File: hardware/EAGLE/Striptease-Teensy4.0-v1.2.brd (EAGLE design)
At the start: 48.3 x 114.3 mm, 18 parts, among them IC1 74245N

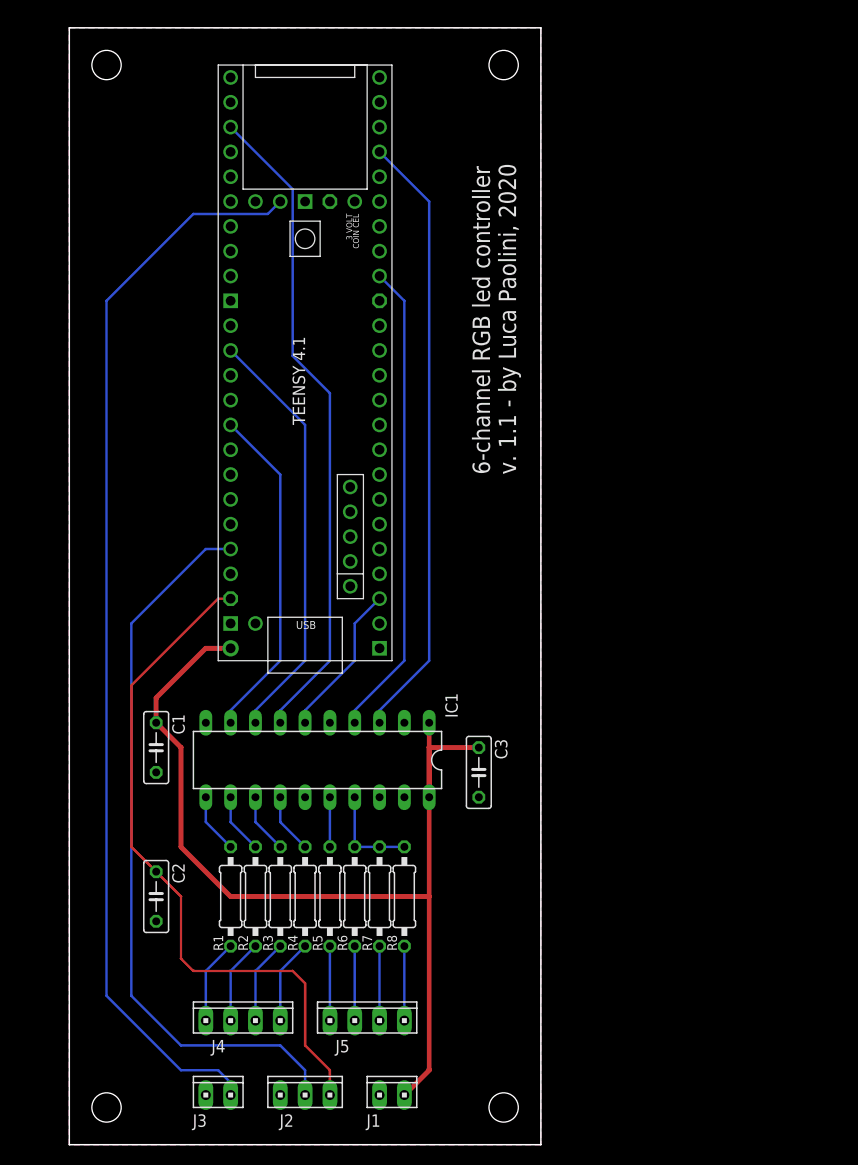
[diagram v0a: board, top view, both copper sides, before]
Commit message: Change connector names in EAGLE boards.
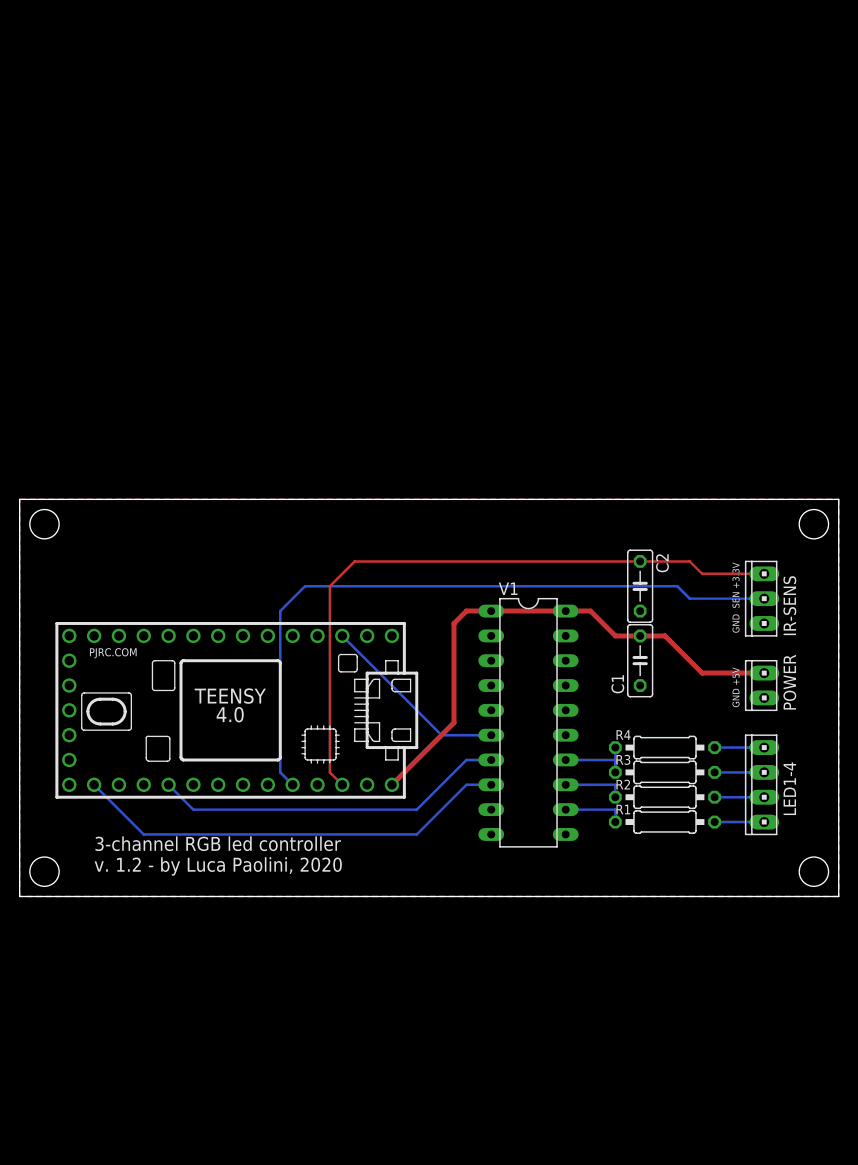
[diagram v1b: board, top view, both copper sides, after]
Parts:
- removed C3: 100n, rcl:C050-025X075
- removed IC1: 74245N, 74ttl-din:DIL20
- removed J1, J3: (no value), con-amp:10X02MTA
- removed J2: (no value), con-amp:10X03MTA
- removed J4, J5: (no value), con-amp:10X04MTA
- removed R5, R6, R7, R8: 100, rcl:0207/10
- removed U$3: TEENSY41-E, teensy:TENNSY41-E
- added IR-SENS: (no value), con-amp:10X03MTA
- added LED1-4: (no value), con-amp:10X04MTA
- added POWER: (no value), con-amp:10X02MTA
- added U$1: TEENSY_4.0-BASIC, Teensy-4.0:TEENSY_4.0-BASIC
- added V1: 74245N, 74ttl-din:DIL20
- moved C2 58.8 mm to (62.2, 53.3)
- moved C1 50.3 mm to (62.2, 45.7), turned to 90 degrees
- moved R1 45.1 mm to (64.8, 29.2), turned to 0 degrees
- moved R2 43.1 mm to (64.8, 31.8), turned to 0 degrees
- moved R3 41.4 mm to (64.8, 34.3), turned to 0 degrees
- moved R4 39.9 mm to (64.8, 36.8), turned to 0 degrees
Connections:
- removed net N$16: IC1.14, R4.1
- removed net N$19: J4.1, R4.2
- removed net N$20: J5.4, R5.2
- removed net N$22: J5.3, R6.2
- removed net N$23: IC1.9, U$3.17-A3/TX4/SDA1
- removed net N$24: IC1.8, U$3.14-A0/TX3/SPDIF_OUT
- removed net N$25: IC1.7, U$3.35-TX8
- removed net N$26: IC1.6, U$3.1-TX1/MISO1/CTX2
- removed net N$27: IC1.4, U$3.24-A10/TX6/SCL2
- removed net N$28: IC1.3, U$3.29-TX7
- removed net N$3: IC1.16, R5.1
- removed net N$31: J2.2, U$3.22-A8/CTX1
- removed net N$6: J5.2, R7.2
- new net N$21: U$1.1/TX, V1.6
- new net N$5: LED1-4.1, R4.2
- net +5V: now also C1.2, POWER.1, U$1.VIN, V1.1, V1.20; no longer C1.1, C3.1, IC1.1, IC1.20, J1.1, U$3.VIN
- net GND: now also C1.1, IR-SENS.3, POWER.2, U$1.GND, U$1.GND2, V1.10, V1.19, V1.2, V1.3, V1.4, V1.5, V1.9; no longer C1.2, C3.2, IC1.10, IC1.19, IC1.2, IC1.5, J1.2, J2.3, J3.2, U$3.GND1, U$3.GND2, U$3.GND3, U$3.GND6
- net N$1: now also IR-SENS.2, U$1.22/A8; no longer C2.1, J2.1, U$3.3V3-3
- net N$10: now also U$1.14/A0, V1.8; no longer J5.1, R8.2
- net N$11: now also V1.12; no longer IC1.11
- net N$12: now also V1.13; no longer IC1.12
- net N$13: now also R4.1, V1.14; no longer IC1.13
- net N$14: now also U$1.17/A3, V1.7; no longer IC1.17, R6.1, R7.1, R8.1
- net N$2: now also C2.1, IR-SENS.1, U$1.3V3_LO; no longer J3.1, U$3.PROGRAM
- net N$7: now also LED1-4.2; no longer J4.2
- net N$8: now also LED1-4.3; no longer J4.3
- net N$9: now also LED1-4.4; no longer J4.4
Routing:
- net N$31: track 74.9 -> 0.00 mm
- net N$25: track 67.3 -> 0.00 mm
- net N$28: track 62.6 -> 0.00 mm
- net N$27: track 48.9 -> 0.00 mm
- net +5V: track 102.8 -> 55.3 mm
- net N$2: track 110.8 -> 66.9 mm
- net N$24: track 43.4 -> 0.00 mm
- net N$10: track 7.62 -> 44.8 mm
- net N$23: track 34.7 -> 0.00 mm
- net N$14: track 10.2 -> 36.2 mm
- net N$21: track 0.00 -> 20.7 mm
- net N$26: track 15.9 -> 0.00 mm
- net N$19: track 8.67 -> 0.00 mm
- net N$6: track 7.62 -> 0.00 mm
- net N$22: track 7.62 -> 0.00 mm
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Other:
- board size 48.3 x 114.3 mm -> 83.8 x 40.6 mm
- board text added: "3-channel RGB led controller v. 1.2 - by Luca Paolini, 2020"
- board text added: "GND +5V"
- board text added: "GND SEN +3.3V"
- board text removed: "6-channel RGB led controller v. 1.1 - by Luca Paolini, 2020"

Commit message: Add connector pinout for LEDs in EAGLE boards.
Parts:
- renumbered IR-SENS to IR-RECV
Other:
- board text added: "1 2 3 3"
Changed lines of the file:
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@@
 <text x="72.39" y="48.26" size="0.7" layer="25" font="vector" rot="R90"> GND  SEN +3.3V</text>
 <text x="72.39" y="40.64" size="0.7" layer="25" font="vector" rot="R90"> GND +5V</text>
+<text x="72.39" y="27.94" size="0.9" layer="25" font="vector" rot="R90">  1    2    3    3</text>
 </plain>
 <attributes>
@@
 <attribute name="VALUE" x="72.7791" y="28.0439" size="1.27" layer="27" rot="R90"/>
 </element>
-<element name="IR-SENS" library="con-amp" library_urn="urn:adsk.eagle:library:127" package="10X03MTA" package3d_urn="urn:adsk.eagle:package:8081621/1" value="" x="74.93" y="52.07" smashed="yes" rot="R90">
+<element name="IR-RECV" library="con-amp" library_urn="urn:adsk.eagle:library:127" package="10X03MTA" package3d_urn="urn:adsk.eagle:package:8081621/1" value="" x="74.93" y="52.07" smashed="yes" rot="R90">
 <attribute name="NAME" x="78.1812" y="48.1838" size="1.27" layer="25" font="vector" rot="R90"/>
 <attribute name="POPULARITY" value="2" x="74.93" y="52.07" size="1.778" layer="27" rot="R90" display="off"/>
@@
 <signal name="N$1">
 <contactref element="U$1" pad="22/A8"/>
-<contactref element="IR-SENS" pad="2"/>
+<contactref element="IR-RECV" pad="2"/>
 <wire x1="74.93" y1="52.07" x2="67.31" y2="52.07" width="0.254" layer="16"/>
 <wire x1="67.31" y1="52.07" x2="66.04" y2="53.34" width="0.254" layer="16"/>
@@
 <wire x1="68.58" y1="54.61" x2="67.31" y2="55.88" width="0.254" layer="1"/>
 <wire x1="67.31" y1="55.88" x2="62.23" y2="55.88" width="0.254" layer="1"/>
-<contactref element="IR-SENS" pad="1"/>
+<contactref element="IR-RECV" pad="1"/>
 <wire x1="31.75" y1="33.02" x2="30.48" y2="34.29" width="0.254" layer="1"/>
 <wire x1="30.48" y1="34.29" x2="30.48" y2="53.34" width="0.254" layer="1"/>
@@
 <signal name="GND">
 <contactref element="V1" pad="10"/>
-<contactref element="IR-SENS" pad="3"/>
+<contactref element="IR-RECV" pad="3"/>
 <contactref element="POWER" pad="2"/>
 <contactref element="U$1" pad="GND2"/>
